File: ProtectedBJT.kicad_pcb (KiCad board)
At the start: 2 copper layers, 38.1 x 38.1 mm, 32 parts, among them P1 CONN_01X04, Q1 BC856, Q2 BC850, Q3 BC856, Q4 BC850, Q5 BC856, Q6 TIP141

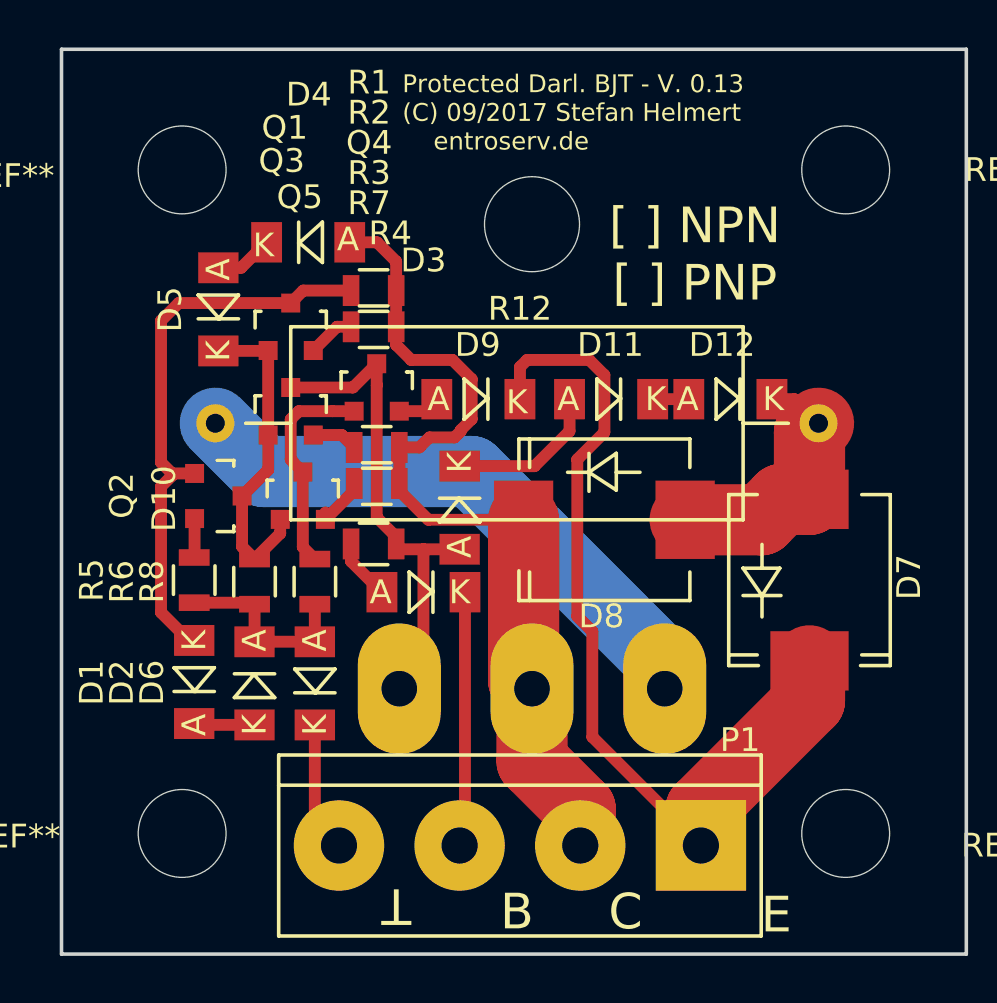
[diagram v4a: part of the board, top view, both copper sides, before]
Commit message: left top hole with more spacing
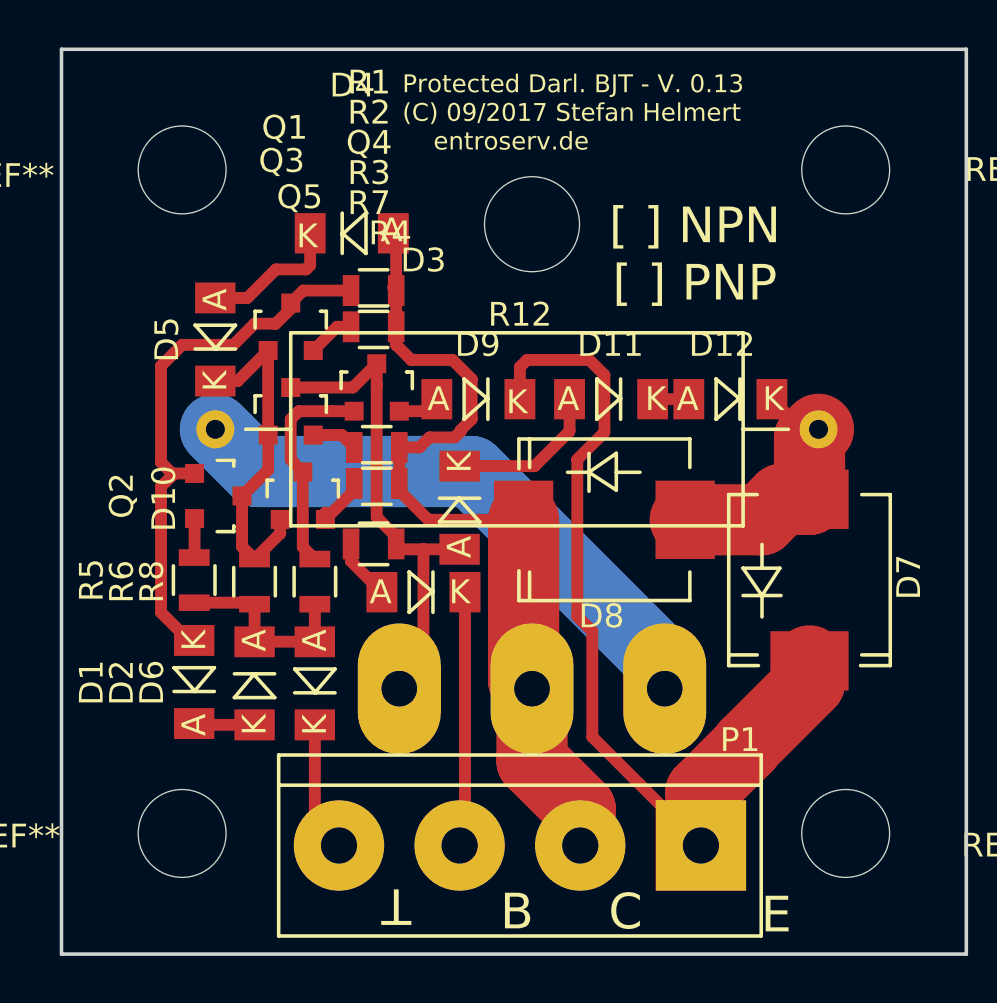
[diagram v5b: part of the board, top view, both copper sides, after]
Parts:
- moved D4 1.87 mm to (129.1, 61.1)
- moved D5 1.28 mm to (123.3, 65.6)
- moved R12 0.25 mm to (136.0, 69.3)
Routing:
- net Net-(D4-Pad1): track 2.48 -> 6.11 mm
- net Net-(D1-Pad2): track 24.0 -> 23.1 mm
- net Net-(D4-Pad2): track 37.1 -> 36.2 mm
- net Net-(D5-Pad1): track 14.0 -> 14.7 mm
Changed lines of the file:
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@@
     (thickness 1.6)
     (drawings 18)
-    (tracks 126)
+    (tracks 137)
     (zones 0)
     (modules 32)
@@
   )
   (module Resistors_ThroughHole:Resistor_Ceramic_Horizontal_L19mm-W8mm-H8mm-p25mm (layer F.Cu)
-    (at 136.017 69.088)
+    (at 136.017 69.342)
     (descr "Resistor, Ceramic, Horizontal")
     (tags "Resistor, Ceramic, Horizontal")
@@
   )
   (module Diodes_SMD:MiniMELF_Standard (layer F.Cu)
-    (at 127.22606 61.468)
+    (at 129.05994 61.087)
     (descr "Diode Mini-MELF Standard")
     (tags "Diode Mini-MELF Standard")
@@
   )
   (module Diodes_SMD:MiniMELF_Standard (layer F.Cu)
-    (at 123.444 64.28994 90)
+    (at 123.317 65.55994 90)
     (descr "Diode Mini-MELF Standard")
     (tags "Diode Mini-MELF Standard")
@@
   (segment (start 129.032 74.90206) (end 130.32994 76.2) (width 0.5) (layer F.Cu) (net 7))
   (segment (start 130.048 75.91806) (end 130.32994 76.2) (width 0.5) (layer F.Cu) (net 7))
-  (segment (start 123.444 62.53988) (end 124.40412 62.53988) (width 0.5) (layer F.Cu) (net 8))
-  (segment (start 124.40412 62.53988) (end 125.476 61.468) (width 0.5) (layer F.Cu) (net 8))
+  (segment (start 127.30988 61.087) (end 127.30988 62.43663) (width 0.5) (layer F.Cu) (net 8))
+  (segment (start 127.30988 62.43663) (end 127.13551 62.611) (width 0.5) (layer F.Cu) (net 8))
+  (segment (start 127.13551 62.611) (end 125.86551 62.611) (width 0.5) (layer F.Cu) (net 8))
+  (segment (start 123.317 63.80988) (end 124.66663 63.80988) (width 0.5) (layer F.Cu) (net 8))
+  (segment (start 124.66663 63.80988) (end 125.86551 62.611) (width 0.5) (layer F.Cu) (net 8))
+  (segment (start 123.317 63.80988) (end 123.51639 63.80988) (width 0.5) (layer F.Cu) (net 8))
   (segment (start 127.508 81.788) (end 127.508 85.852) (width 0.5) (layer F.Cu) (net 9))
   (segment (start 127.508 85.852) (end 128.524 86.868) (width 0.5) (layer F.Cu) (net 9))
+  (segment (start 145.69007 82.65593) (end 148.336 80.01) (width 3) (layer F.Cu) (net 10))
+  (segment (start 148.336 80.01) (end 148.336 79.09306) (width 3) (layer F.Cu) (net 10))
+  (segment (start 143.764 84.619895) (end 145.69007 82.693825) (width 3) (layer F.Cu) (net 10))
+  (segment (start 145.69007 82.693825) (end 145.69007 82.65593) (width 3) (layer F.Cu) (net 10))
+  (segment (start 143.764 86.868) (end 143.764 84.619895) (width 3) (layer F.Cu) (net 10))
   (segment (start 143.764 86.868) (end 139.192 82.296) (width 0.5) (layer F.Cu) (net 10))
   (segment (start 139.192 82.296) (end 139.192 77.851) (width 0.5) (layer F.Cu) (net 10))
@@
   (segment (start 136.144 66.72237) (end 136.144 68.072) (width 0.5) (layer F.Cu) (net 10))
   (segment (start 136.144 67.87261) (end 136.144 68.072) (width 0.5) (layer F.Cu) (net 10))
-  (segment (start 148.336 80.772) (end 148.336 79.09306) (width 3) (layer F.Cu) (net 10))
-  (segment (start 143.764 85.344) (end 148.336 80.772) (width 3) (layer F.Cu) (net 10))
-  (segment (start 143.764 86.868) (end 143.764 85.344) (width 3) (layer F.Cu) (net 10))
   (segment (start 127.442 69.58076) (end 128.64076 69.58076) (width 0.5) (layer F.Cu) (net 11))
   (segment (start 128.64076 69.58076) (end 129.164 70.104) (width 0.5) (layer F.Cu) (net 11))
+  (segment (start 121.031 70.739) (end 121.031 66.675) (width 0.5) (layer F.Cu) (net 12))
+  (segment (start 126.492 64.02578) (end 126.492 64.262) (width 0.5) (layer F.Cu) (net 12))
+  (segment (start 126.492 64.262) (end 125.857 64.897) (width 0.5) (layer F.Cu) (net 12))
+  (segment (start 125.857 64.897) (end 124.968 64.897) (width 0.5) (layer F.Cu) (net 12))
+  (segment (start 124.968 64.897) (end 124.079 65.786) (width 0.5) (layer F.Cu) (net 12))
+  (segment (start 124.079 65.786) (end 121.92 65.786) (width 0.5) (layer F.Cu) (net 12))
+  (segment (start 121.92 65.786) (end 121.031 66.675) (width 0.5) (layer F.Cu) (net 12))
   (segment (start 121.49324 71.20124) (end 121.031 70.739) (width 0.5) (layer F.Cu) (net 12))
-  (segment (start 121.031 64.77) (end 121.77522 64.02578) (width 0.5) (layer F.Cu) (net 12))
-  (segment (start 121.031 70.739) (end 121.031 64.77) (width 0.5) (layer F.Cu) (net 12))
-  (segment (start 121.77522 64.02578) (end 126.492 64.02578) (width 0.5) (layer F.Cu) (net 12))
   (segment (start 121.49324 71.20124) (end 121.49324 71.29276) (width 0.5) (layer F.Cu) (net 12))
   (segment (start 121.49324 71.29276) (end 121.031 71.755) (width 0.5) (layer F.Cu) (net 12))
@@
   (segment (start 127.508 78.28788) (end 124.968 78.28788) (width 0.5) (layer F.Cu) (net 13))
   (segment (start 127.508 76.708) (end 127.508 78.28788) (width 0.5) (layer F.Cu) (net 13))
-  (segment (start 128.97612 61.468) (end 130.12636 61.468) (width 0.5) (layer F.Cu) (net 14))
-  (segment (start 130.12636 61.468) (end 130.932 62.27364) (width 0.5) (layer F.Cu) (net 14))
-  (segment (start 130.932 62.27364) (end 130.932 63.5) (width 0.5) (layer F.Cu) (net 14))
+  (segment (start 130.932 63.5) (end 130.932 61.209) (width 0.5) (layer F.Cu) (net 14))
+  (segment (start 130.932 61.209) (end 130.81 61.087) (width 0.5) (layer F.Cu) (net 14))
+  (segment (start 130.80149 63.36949) (end 130.932 63.5) (width 0.5) (layer F.Cu) (net 14))
   (segment (start 130.932 65.024) (end 130.932 65.788918) (width 0.5) (layer F.Cu) (net 14))
   (segment (start 130.932 65.788918) (end 131.564082 66.421) (width 0.5) (layer F.Cu) (net 14))
@@
   (segment (start 136.29894 73.152) (end 136.29894 79.91094) (width 3) (layer F.Cu) (net 14))
   (segment (start 136.29894 79.91094) (end 136.652 80.264) (width 3) (layer F.Cu) (net 14))
+  (segment (start 123.317 67.31) (end 124.25676 67.31) (width 0.5) (layer F.Cu) (net 15))
+  (segment (start 124.25676 67.31) (end 125.542 66.02476) (width 0.5) (layer F.Cu) (net 15))
   (segment (start 125.542 69.58076) (end 125.542 71.05146) (width 0.5) (layer F.Cu) (net 15))
   (segment (start 125.542 71.05146) (end 124.44222 72.15124) (width 0.5) (layer F.Cu) (net 15))
-  (segment (start 123.444 66.04) (end 125.52676 66.04) (width 0.5) (layer F.Cu) (net 15))
   (segment (start 125.52676 66.04) (end 125.542 66.02476) (width 0.5) (layer F.Cu) (net 15))
   (segment (start 125.542 69.58076) (end 125.542 66.02476) (width 0.5) (layer F.Cu) (net 15))
@@
   (segment (start 124.44222 74.28222) (end 124.968 74.808) (width 0.5) (layer F.Cu) (net 15))
   (segment (start 125.268 74.808) (end 124.968 74.808) (width 0.5) (layer F.Cu) (net 15))
-  (segment (start 146.75612 68.072) (end 147.701 68.072) (width 0.5) (layer F.Cu) (net 16))
-  (segment (start 147.701 68.072) (end 148.717 69.088) (width 0.5) (layer F.Cu) (net 16))
-  (segment (start 148.336 72.29094) (end 148.336 69.469) (width 3) (layer F.Cu) (net 16))
-  (segment (start 148.336 69.469) (end 148.717 69.088) (width 3) (layer F.Cu) (net 16))
+  (segment (start 148.336 72.29094) (end 148.336 69.723) (width 3) (layer F.Cu) (net 16))
+  (segment (start 148.336 69.723) (end 148.717 69.342) (width 3) (layer F.Cu) (net 16))
+  (segment (start 148.717 69.342) (end 148.02612 69.342) (width 0.5) (layer F.Cu) (net 16))
+  (segment (start 148.02612 69.342) (end 146.75612 68.072) (width 0.5) (layer F.Cu) (net 16))
   (segment (start 146.75612 68.072) (end 146.75612 68.27139) (width 0.5) (layer F.Cu) (net 16))
   (segment (start 147.16506 72.29094) (end 146.304 73.152) (width 3) (layer F.Cu) (net 16))
@@
   (segment (start 142.24 80.264) (end 142.24 79.26324) (width 3) (layer B.Cu) (net 21))
   (segment (start 142.24 79.26324) (end 134.09676 71.12) (width 3) (layer B.Cu) (net 21))
-  (segment (start 134.09676 71.12) (end 125.349 71.12) (width 3) (layer B.Cu) (net 21))
-  (segment (start 125.349 71.12) (end 123.317 69.088) (width 3) (layer B.Cu) (net 21))
+  (segment (start 134.09676 71.12) (end 125.095 71.12) (width 3) (layer B.Cu) (net 21))
+  (segment (start 125.095 71.12) (end 123.317 69.342) (width 3) (layer B.Cu) (net 21))
   (zone (net 9) (net_name GND) (layer F.Cu) (hatch edge 0.508)
     (connect_pads (clearance 0.508))
